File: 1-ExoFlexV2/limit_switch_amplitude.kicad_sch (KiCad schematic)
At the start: 36 parts, among them U21 SN74LVC3G14DCUT_V2, U22 SN74LVC3G14DCUT_V2, U23 SN74LVC3G14DCUT_V2, U24 SN74LVC3G14DCUT_V2, U25 SN74LVC3G14DCUT_V2, U26 SN74LVC3G14DCUT_V2, U27 SN74LVC3G14DCUT_V2, U28 SN74LVC1G32DBVR, U29 SN74LVC1G32DBVR

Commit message: Schématisation terminée
- Schéma terminé
- Passage vers le PCB
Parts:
- C28: renamed from C45; value 10uF -> 10uF 10V X7R; DESCRIPTION (none) -> 10 µF ±10% 10V Ceramic Capacitor X7R 0805 (2012 Metric); MANUFACTURER (none) -> Murata Electronics; PACKAGE (none) -> 0805 (2012 Metric); PART NUMBER (none) -> GRM21BR71A106KA73L; TYPE (none) -> SMD
- C29, C30, C31, C32, C33, C34: renamed from C?; value 10uF -> 10uF 10V X7R; DESCRIPTION (none) -> 10 µF ±10% 10V Ceramic Capacitor X7R 0805 (2012 Metric); MANUFACTURER (none) -> Murata Electronics; PACKAGE (none) -> 0805 (2012 Metric); PART NUMBER (none) -> GRM21BR71A106KA73L; TYPE (none) -> SMD
- J89, J90, J91: renamed from J?; value Jmp -> Jumper; footprint (none) -> Connector_PinSocket_2.54mm:PinSocket_1x03_P2.54mm_Vertical; DESCRIPTION (none) -> CONN HEADER VERT 3POS 2.54MM; MANUFACTURER (none) -> Würth Elektronik; PACKAGE (none) -> Square 0.100" (2.54mm); PART NUMBER (none) -> 61300311121; TYPE (none) -> Through Hole
- R100, R101, R102, R103, R110, R98: renamed from R?; value 10k -> 10k 5% 1/8W; DESCRIPTION (none) -> 10 kOhms ±5% 0.125W, 1/8W Chip Resistor 0805 (2012 Metric) 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; MANUFACTURER (none) -> Panasonic Electronic Components; PACKAGE (none) -> 0805 (2012 Metric); PART NUMBER (none) -> ERJ-6GEYJ103V; TYPE (none) -> SMD
- R104: renamed from R49; value 5k -> 5,1k 5% 1/8W; DESCRIPTION (none) -> 5.1 kOhms ±5% 0.125W, 1/8W Chip Resistor 0805 (2012 Metric)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; MANUFACTURER (none) -> Panasonic Electronic Components; PACKAGE (none) -> 0805 (2012 Metric); PART NUMBER (none) -> ERJ-6GEYJ512V; TYPE (none) -> SMD
- R105, R106, R107, R108, R109, R111: renamed from R?; value 5k -> 5,1k 5% 1/8W; DESCRIPTION (none) -> 5.1 kOhms ±5% 0.125W, 1/8W Chip Resistor 0805 (2012 Metric)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; MANUFACTURER (none) -> Panasonic Electronic Components; PACKAGE (none) -> 0805 (2012 Metric); PART NUMBER (none) -> ERJ-6GEYJ512V; TYPE (none) -> SMD
- R112, R113, R114: renamed from R?; value 100k -> 100k 5% 1/8W; DESCRIPTION (none) -> 100 kOhms ±5% 0.125W, 1/8W Chip Resistor 0805 (2012 Metric)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; MANUFACTURER (none) -> Panasonic Electronic Components; PACKAGE (none) -> 0805 (2012 Metric); PART NUMBER (none) -> ERJ-6GEYJ104V; TYPE (none) -> SMD
- R99: renamed from R43; value 10k -> 10k 5% 1/8W; DESCRIPTION (none) -> 10 kOhms ±5% 0.125W, 1/8W Chip Resistor 0805 (2012 Metric) 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; MANUFACTURER (none) -> Panasonic Electronic Components; PACKAGE (none) -> 0805 (2012 Metric); PART NUMBER (none) -> ERJ-6GEYJ103V; TYPE (none) -> SMD
- U42: renamed from U23; value SN74LVC3G14DCUT_V2 -> Inverter; DESCRIPTION (none) -> Inverter IC 3 Channel Schmitt Trigger 8-VSSOP; MANUFACTURER (none) -> Texas Instruments; PACKAGE (none) -> 8-VFSOP (0.091", 2.30mm Width); PART NUMBER (none) -> SN74LVC3G14DCUT; TYPE (none) -> SMD
- U43: renamed from U21; value SN74LVC3G14DCUT_V2 -> Inverter; DESCRIPTION (none) -> Inverter IC 3 Channel Schmitt Trigger 8-VSSOP; MANUFACTURER (none) -> Texas Instruments; PACKAGE (none) -> 8-VFSOP (0.091", 2.30mm Width); PART NUMBER (none) -> SN74LVC3G14DCUT; TYPE (none) -> SMD
- U44: renamed from U22; value SN74LVC3G14DCUT_V2 -> Inverter; DESCRIPTION (none) -> Inverter IC 3 Channel Schmitt Trigger 8-VSSOP; MANUFACTURER (none) -> Texas Instruments; PACKAGE (none) -> 8-VFSOP (0.091", 2.30mm Width); PART NUMBER (none) -> SN74LVC3G14DCUT; TYPE (none) -> SMD
- U45: renamed from U24; value SN74LVC3G14DCUT_V2 -> Inverter; DESCRIPTION (none) -> Inverter IC 3 Channel Schmitt Trigger 8-VSSOP; MANUFACTURER (none) -> Texas Instruments; PACKAGE (none) -> 8-VFSOP (0.091", 2.30mm Width); PART NUMBER (none) -> SN74LVC3G14DCUT; TYPE (none) -> SMD
- U46: renamed from U25; value SN74LVC3G14DCUT_V2 -> Inverter; DESCRIPTION (none) -> Inverter IC 3 Channel Schmitt Trigger 8-VSSOP; MANUFACTURER (none) -> Texas Instruments; PACKAGE (none) -> 8-VFSOP (0.091", 2.30mm Width); PART NUMBER (none) -> SN74LVC3G14DCUT; TYPE (none) -> SMD
- U47: renamed from U26; value SN74LVC3G14DCUT_V2 -> Inverter; DESCRIPTION (none) -> Inverter IC 3 Channel Schmitt Trigger 8-VSSOP; MANUFACTURER (none) -> Texas Instruments; PACKAGE (none) -> 8-VFSOP (0.091", 2.30mm Width); PART NUMBER (none) -> SN74LVC3G14DCUT; TYPE (none) -> SMD
- U48: renamed from U27; value SN74LVC3G14DCUT_V2 -> Inverter; DESCRIPTION (none) -> Inverter IC 3 Channel Schmitt Trigger 8-VSSOP; MANUFACTURER (none) -> Texas Instruments; PACKAGE (none) -> 8-VFSOP (0.091", 2.30mm Width); PART NUMBER (none) -> SN74LVC3G14DCUT; TYPE (none) -> SMD
- U49: renamed from U28; value SN74LVC1G32DBVR -> OR Gate; DESCRIPTION (none) -> OR Gate IC 1 Channel SOT-23-5; MANUFACTURER (none) -> Texas Instruments; PACKAGE (none) -> SC-74A, SOT-753; PART NUMBER (none) -> SN74LVC1G32DBVR; TYPE (none) -> SMD
- U50: renamed from U29; value SN74LVC1G32DBVR -> OR Gate; DESCRIPTION (none) -> OR Gate IC 1 Channel SOT-23-5; MANUFACTURER (none) -> Texas Instruments; PACKAGE (none) -> SC-74A, SOT-753; PART NUMBER (none) -> SN74LVC1G32DBVR; TYPE (none) -> SMD
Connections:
- net MIN_SW_1: now also R101.1
- net MIN_SW_3: now also R103.1
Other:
- note added: "2xOrGate : 5V @ 64,02mA 7xNOTGte : 5V @ 224,07mA 7x10k : 5V @ 3,5mA 3x200k : 5V @ 0,15mA Total current : 5VA @ 296mA"
- note removed: "2xOrGate : 5V @ 64,02mA 7xNOTGte : 5V @ 224,07mA 7x10k : 5V @ 3,5mA 3x200k : 5V @ 0,075mA Total current : 5VA @ 295mA"

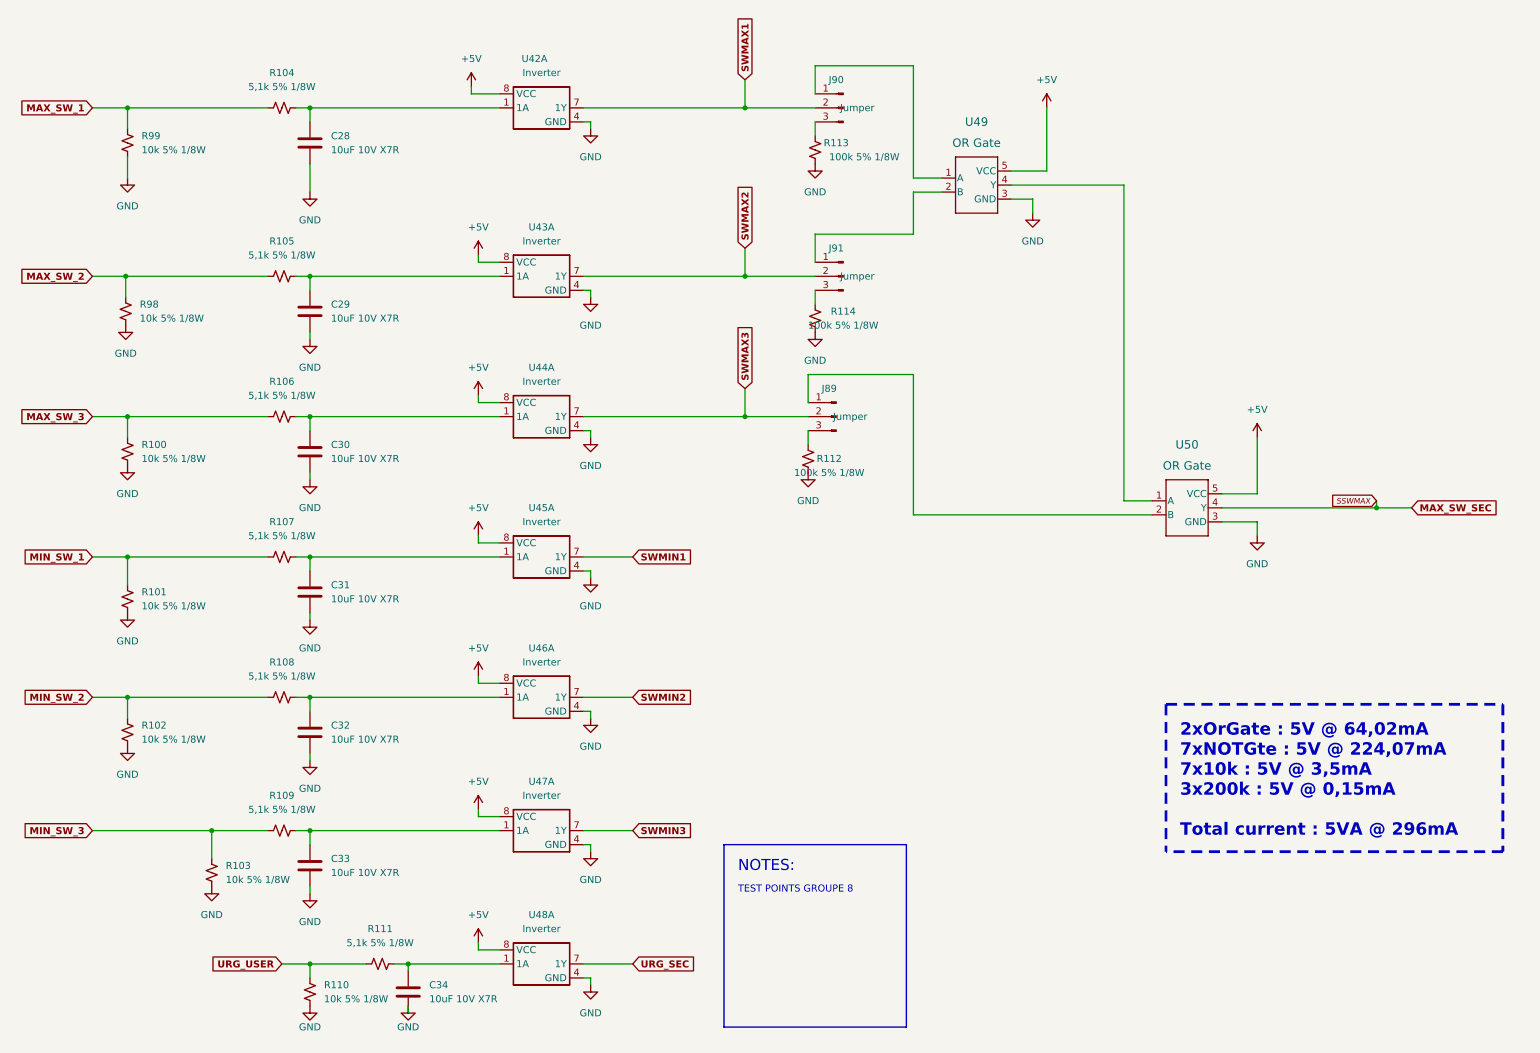
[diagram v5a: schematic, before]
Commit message: Finalisation 3
- Changement des régulateur de tension
- Retrait de test point inutile
- Changement de jumper mal positionner
- Ajout de Mounting holes et fiducial
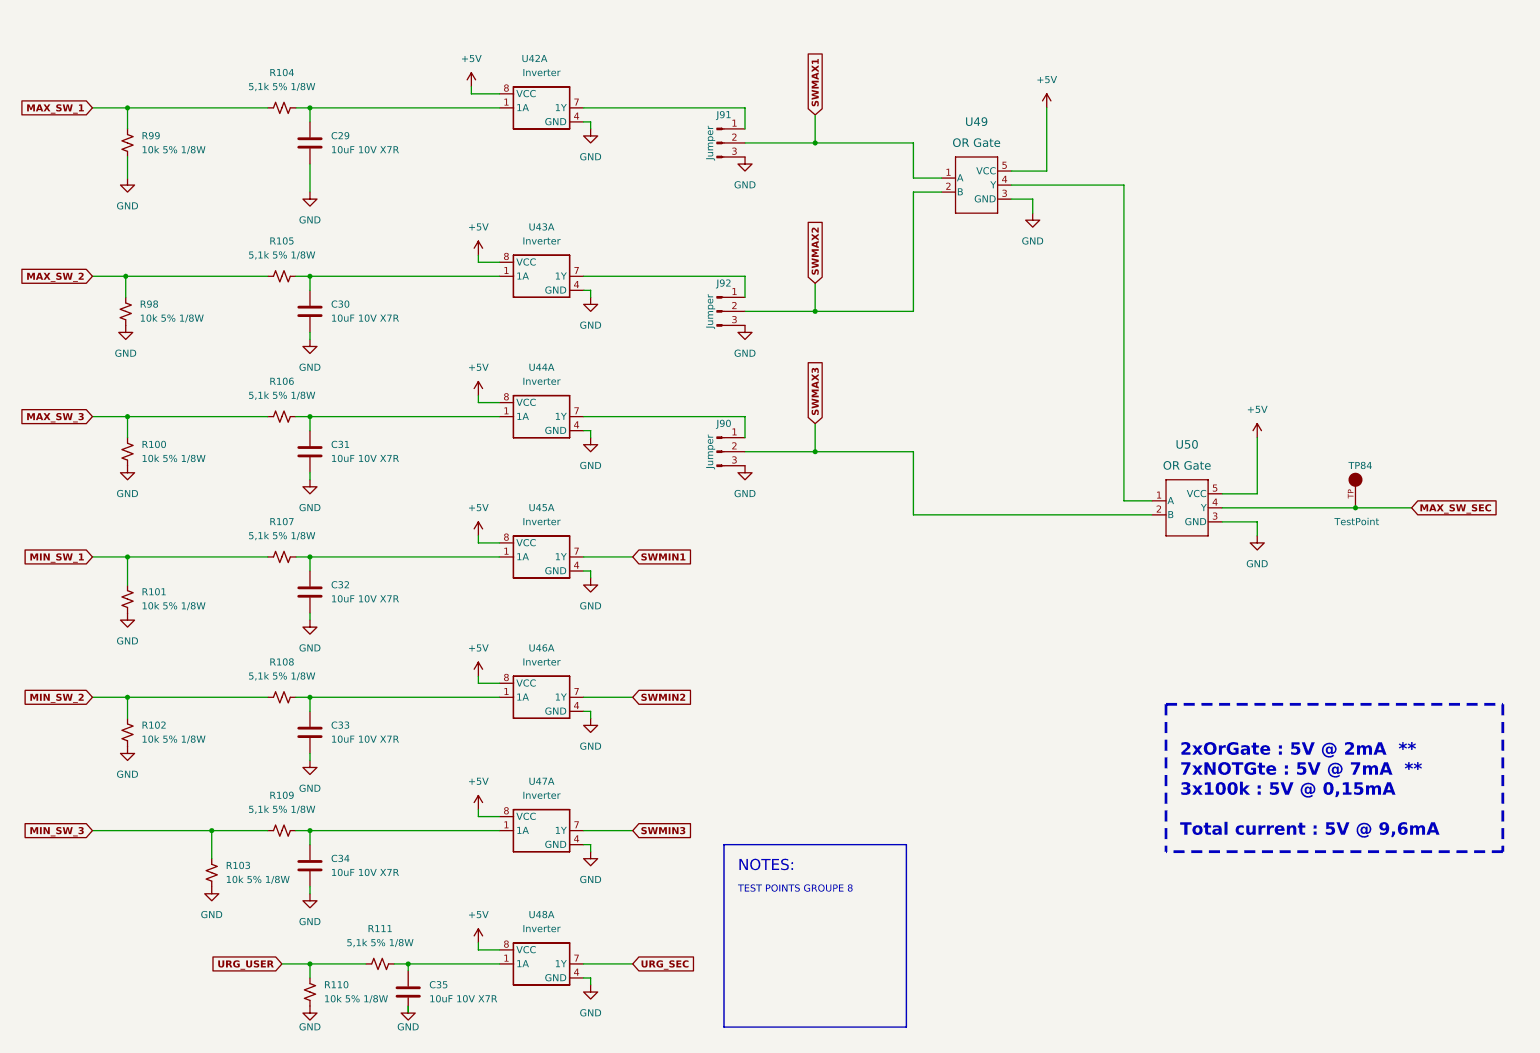
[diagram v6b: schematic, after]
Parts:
- removed R112, R113, R114: 100k 5% 1/8W, Resistor_SMD:R_0805_2012Metric, symbol Device:R_Small_US
- added TP84: TestPoint, FootPrint:KEYSTONE_5005, symbol SymLib:5005
- J90: renamed from J89; footprint Connector_PinSocket_2.54mm:PinSocket_1x03_P2.54mm_Vertical -> Connector_PinHeader_2.54mm:PinHeader_1x03_P2.54mm_Vertical
- J91: renamed from J90; footprint Connector_PinSocket_2.54mm:PinSocket_1x03_P2.54mm_Vertical -> Connector_PinHeader_2.54mm:PinHeader_1x03_P2.54mm_Vertical
- J92: renamed from J91; footprint Connector_PinSocket_2.54mm:PinSocket_1x03_P2.54mm_Vertical -> Connector_PinHeader_2.54mm:PinHeader_1x03_P2.54mm_Vertical
- renumbered C28 to C29, C29 to C30, C30 to C31, C31 to C32, C32 to C33, C33 to C34, C34 to C35
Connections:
- net GND: now also J90.3 (Pin_3), J91.3 (Pin_3), J92.3 (Pin_3)
- net MAX_SW_SEC: now also TP84.TP
- net SWMAX1: now also U49.1 (A); no longer U42.7 (1Y)
- net SWMAX2: now also U49.2 (B); no longer U43.7 (1Y)
- net SWMAX3: now also U50.2 (B); no longer U44.7 (1Y)
- net at J90.1 (Pin_1): now also U44.7 (1Y); no longer U50.2 (B)
- net at J92.1 (Pin_1): now also U43.7 (1Y); no longer U49.2 (B)
- net at J91.1 (Pin_1): now also U42.7 (1Y); no longer U49.1 (A)
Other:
- note added: "2xOrGate : 5V @ 2mA ** 7xNOTGte : 5V @ 7mA ** 3x100k : 5V @ 0,15mA Total current : 5V @ 9,6mA"
- note removed: "2xOrGate : 5V @ 64,02mA 7xNOTGte : 5V @ 224,07mA 7x10k : 5V @ 3,5mA 3x200k : 5V @ 0,15mA Total current : 5VA @ 296mA"
- moved on the sheet: J90, J91, J92

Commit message: Finalisation schéma FIN
- Changement des uméro pour les inverseurs
- Changement des connecteur et début de placement
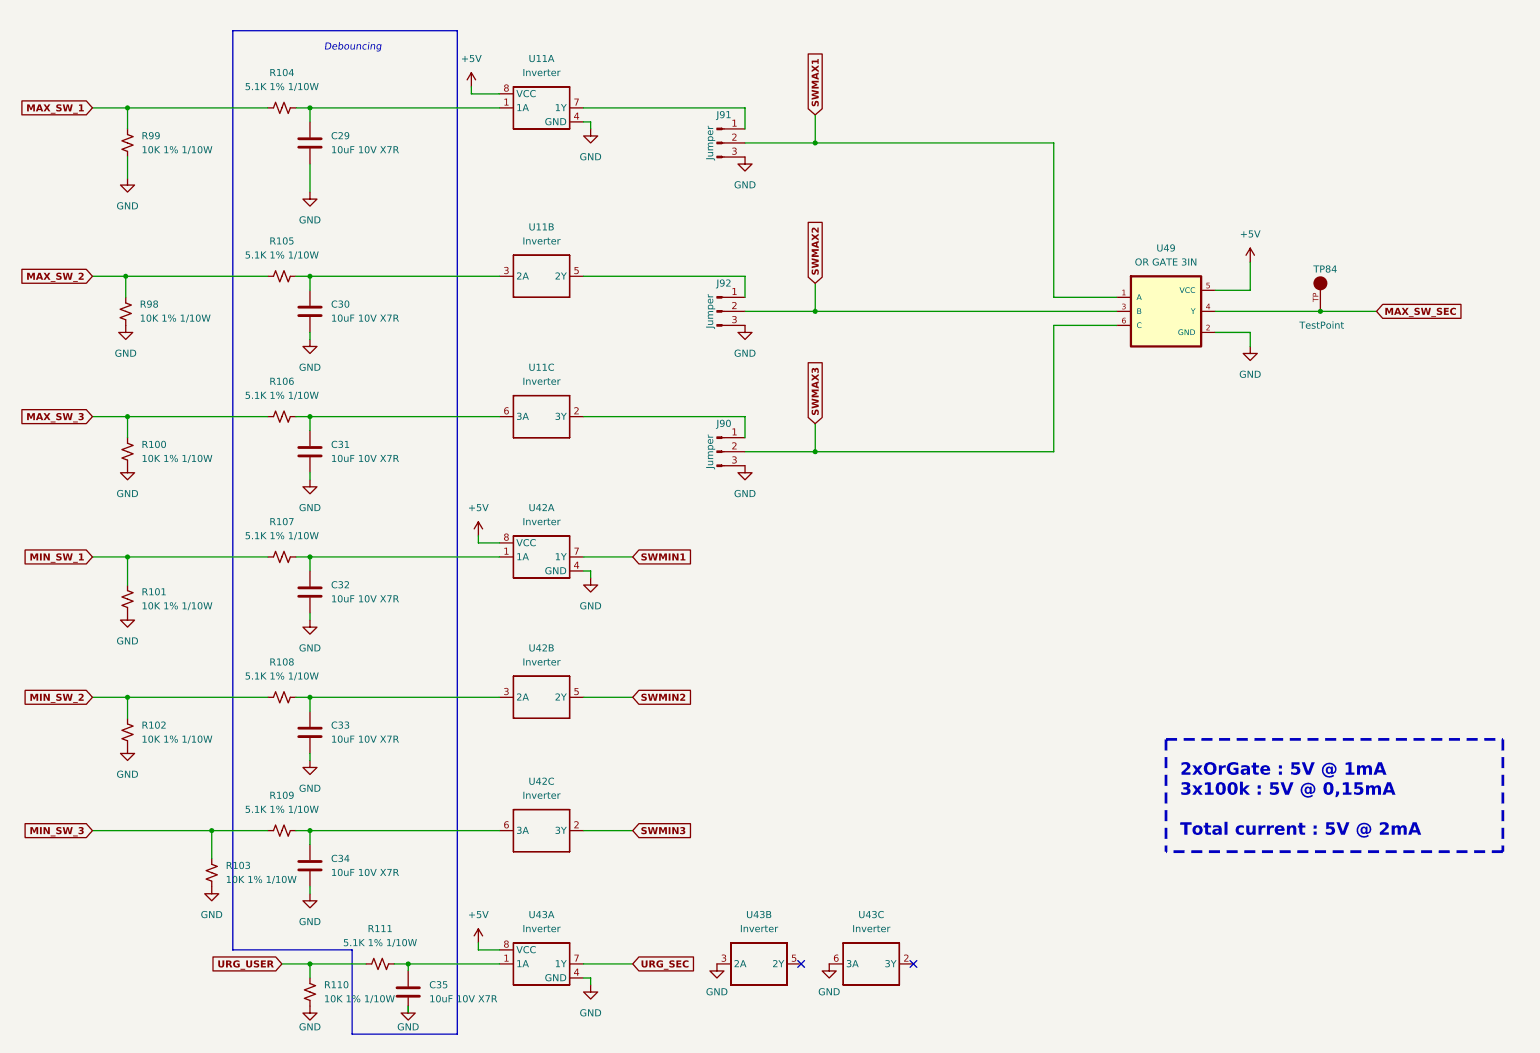
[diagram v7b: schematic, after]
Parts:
- removed U44, U45, U46, U47, U48: Inverter, FootPrint:SN74LVC3G14DCUT, symbol SymLib:SN74LVC3G14DCUT_V2
- removed U49, U50: OR Gate, FootPrint:SOT95P270X145-5N, symbol SymLib:SN74LVC1G32DBVR
- added U11: Inverter, FootPrint:SN74LVC3G14DCUT, symbol SymLib:SN74LVC3G14DCUT_V2
- added unit 2 of U42
- added unit 3 of U42
- added unit 3 of U43
- added unit 2 of U43
- added U49: OR GATE 3IN, FootPrintLib:SOT95P280X145-6N, symbol SymLib:SN74LVC1G332DBVR
- R100, R101, R102, R103, R110, R98, R99: value 10k 5% 1/8W -> 10K 1% 1/10W; footprint Resistor_SMD:R_0805_2012Metric -> Resistor_SMD:R_0603_1608Metric; DESCRIPTION 10 kOhms ±5% 0.125W, 1/8W Chip Resistor 0805 (2012 Metric) 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 -> 10 kOhms ±1% 0.1W, 1/10W Chip Resistor 0603 (1608 Metric) A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; PACKAGE 0805 (2012 Metric) -> 0603 (1608 Metric); PART NUMBER ERJ-6GEYJ103V -> ERJ-3EKF1002V
- R104, R105, R106, R107, R108, R109, R111: value 5,1k 5% 1/8W -> 5.1K 1% 1/10W; footprint Resistor_SMD:R_0805_2012Metric -> Resistor_SMD:R_0603_1608Metric; DESCRIPTION 5.1 kOhms ±5% 0.125W, 1/8W Chip Resistor 0805 (2012 Metric)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 -> 5.1 kOhms ±1% 0.1W, 1/10W Chip Resistor 0603 (1608 Metric) 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; PACKAGE 0805 (2012 Metric) -> 0603 (1608 Metric); PART NUMBER ERJ-6GEYJ512V -> ERJ-3EKF5101V
- TP84: NOTES (none) -> DO NOT POPULATE; PURCHASE-URL https://pricing.snapeda.com/search/part/5005/?ref=eda -> (none)
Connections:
- net +5V: now also U11.8 (VCC), U49.5 (VCC)
- net GND: now also U11.4 (GND), U43.3 (2A), U43.6 (3A), U49.2 (GND)
- net MAX_SW_SEC: now also U49.4 (Y)
- net SWMAX1: now also U49.1 (A)
- net SWMAX2: now also U49.3 (B)
- net SWMAX3: now also U49.6 (C)
- net SWMIN1: now also U42.7 (1Y)
- net SWMIN2: now also U42.5 (2Y)
- net SWMIN3: now also U42.2 (3Y)
- net URG_SEC: now also U43.7 (1Y)
- net at C31.1, R106.2: now also U11.6 (3A)
- net at J90.1 (Pin_1): now also U11.2 (3Y)
- net at C35.1, R111.2: now also U43.1 (1A)
- net at C30.1, R105.2: now also U11.3 (2A); no longer U43.1 (1A)
- net at J92.1 (Pin_1): now also U11.5 (2Y); no longer U43.7 (1Y)
- net at C34.1, R109.2: now also U42.6 (3A)
- net at C32.1, R107.2: now also U42.1 (1A)
- net at C33.1, R108.2: now also U42.3 (2A)
- net at C29.1, R104.2: now also U11.1 (1A); no longer U42.1 (1A)
- net at J91.1 (Pin_1): now also U11.7 (1Y); no longer U42.7 (1Y)
- no-connect marks 0 -> 2
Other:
- note added: "2xOrGate : 5V @ 1mA 3x100k : 5V @ 0,15mA Total current : 5V @ 2mA"
- note added: "Debouncing"
- note removed: "2xOrGate : 5V @ 2mA ** 7xNOTGte : 5V @ 7mA ** 3x100k : 5V @ 0,15mA Total current : 5V @ 9,6mA"
- note removed: "NOTES:"
- note removed: "TEST POINTS GROUPE 8"
- moved on the sheet: TP84
